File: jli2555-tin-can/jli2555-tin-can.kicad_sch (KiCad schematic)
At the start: 20 parts, among them J2 AudioJack3, U1 OPA134, U2 TL072

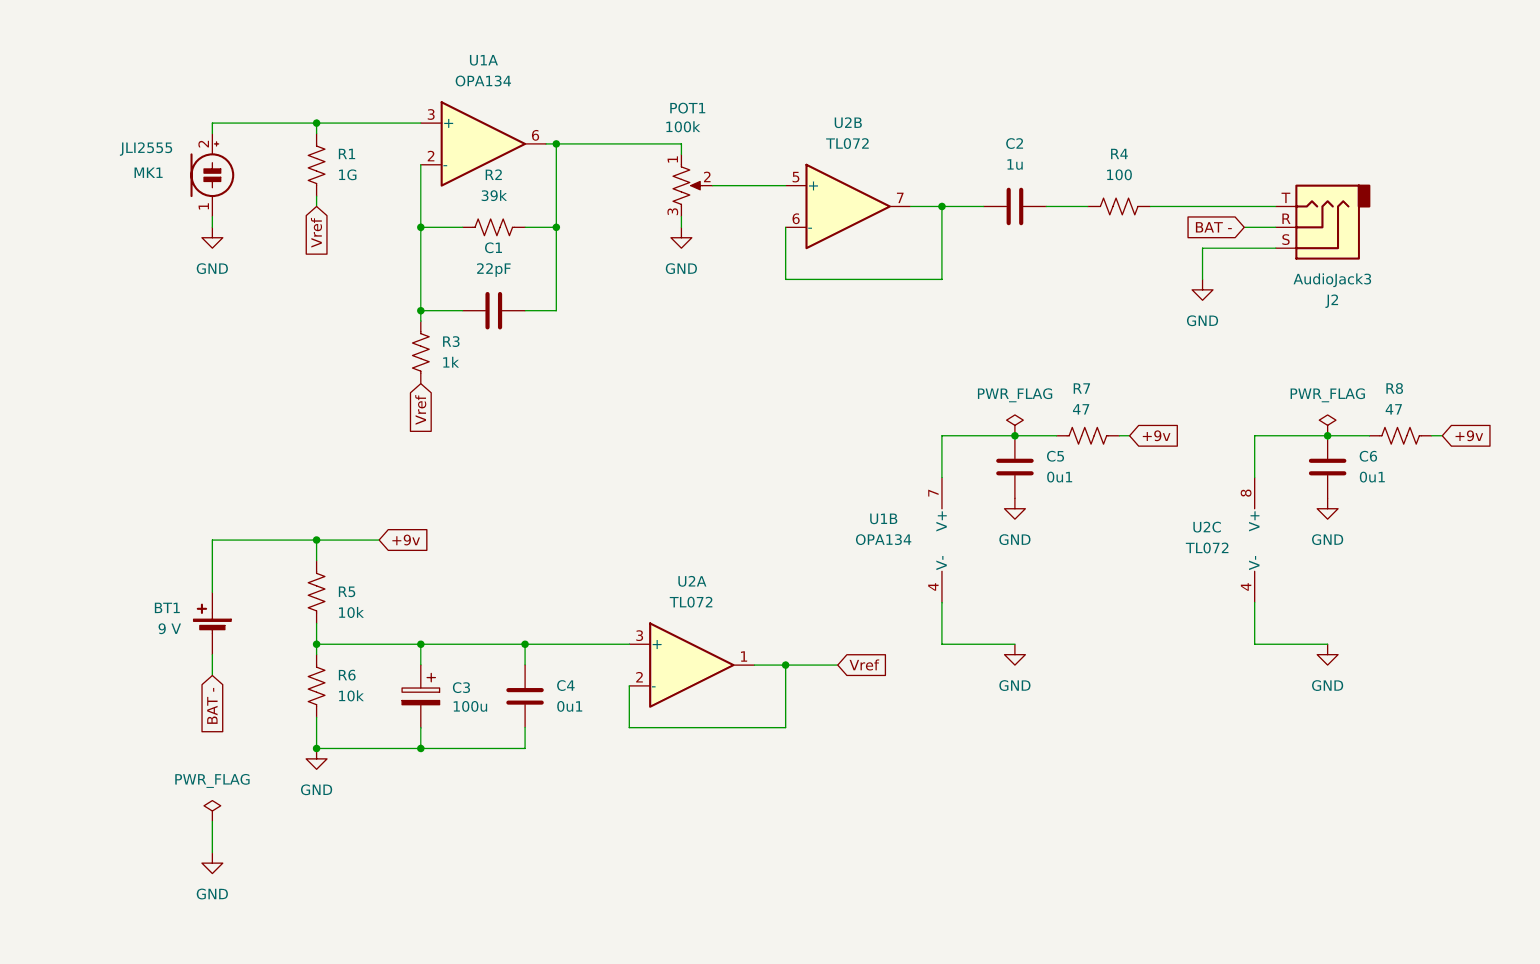
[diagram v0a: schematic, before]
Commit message: finalize the -9v powered circuit design. Renamed entire project
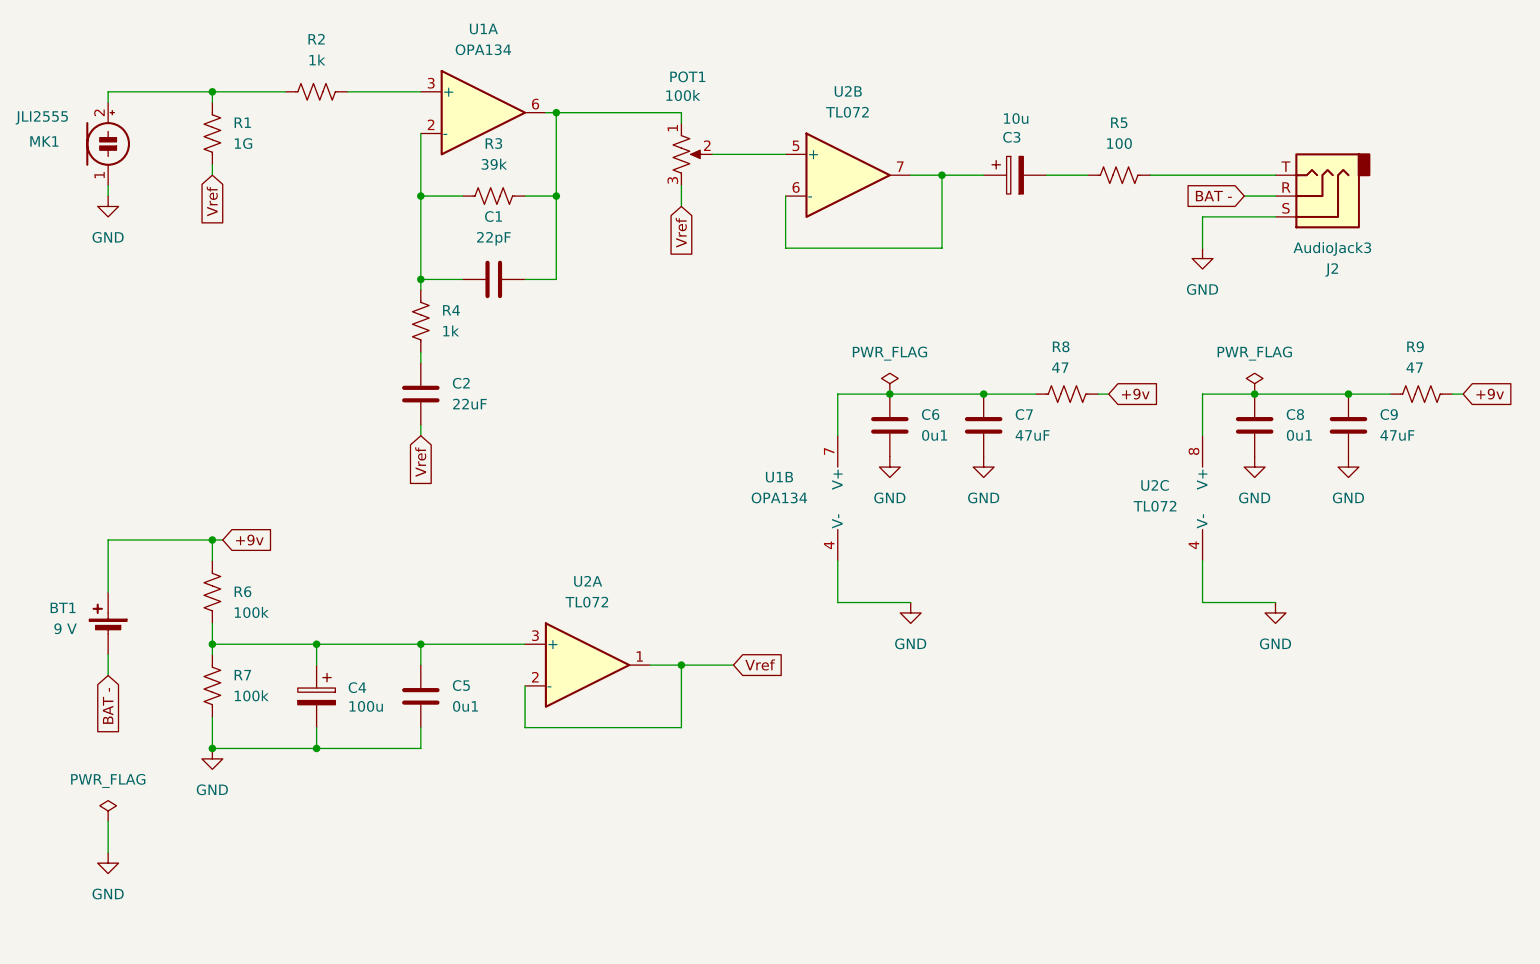
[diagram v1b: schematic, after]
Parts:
- added C3: 10u, Capacitor_THT:CP_Radial_D5.0mm_P2.50mm, symbol Device:C_Polarized
- added C7, C9: 47uF, Capacitor_THT:C_Disc_D5.0mm_W2.5mm_P2.50mm, symbol Device:C
- added R2: 1k, Resistor_THT:R_Axial_DIN0207_L6.3mm_D2.5mm_P10.16mm_Horizontal, symbol Device:R_US
- C2: value 1u -> 22uF; footprint Capacitor_THT:C_Rect_L7.2mm_W4.5mm_P5.00mm_FKS2_FKP2_MKS2_MKP2 -> Capacitor_THT:C_Disc_D5.0mm_W2.5mm_P2.50mm
- R6: renamed from R5; value 10k -> 100k
- R7: renamed from R6; value 10k -> 100k
- renumbered C3 to C4, C4 to C5, C5 to C6, C6 to C8, R2 to R3, R3 to R4, R4 to R5, R7 to R8, R8 to R9
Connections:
- net GND: now also C7.1, C9.1; no longer POT1.3
- net Vref: now also C2.1, POT1.3; no longer R4.2
- net at C8.2, R9.1, U2.8 (V+): now also C9.2
- net at MK1.2 (+), R1.1: now also R2.1; no longer U1.3 (+)
- net at C2.2: now also R4.2; no longer R5.1
- net at U2.6 (-), U2.7: now also C3.1; no longer C2.1
- net at C6.2, R8.1, U1.7 (V+): now also C7.2
- new net: C3.2, R5.1
- new net: R2.2, U1.3 (+)
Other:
- title: JLI 2555 tin can mic  -> JLI 2555 tin can microphone
- moved on the sheet: BT1, C1, C4, C5, C6, C8, J2, MK1, POT1, R1, R3, R4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

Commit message: Finalization of the first printed prototype, revision 1
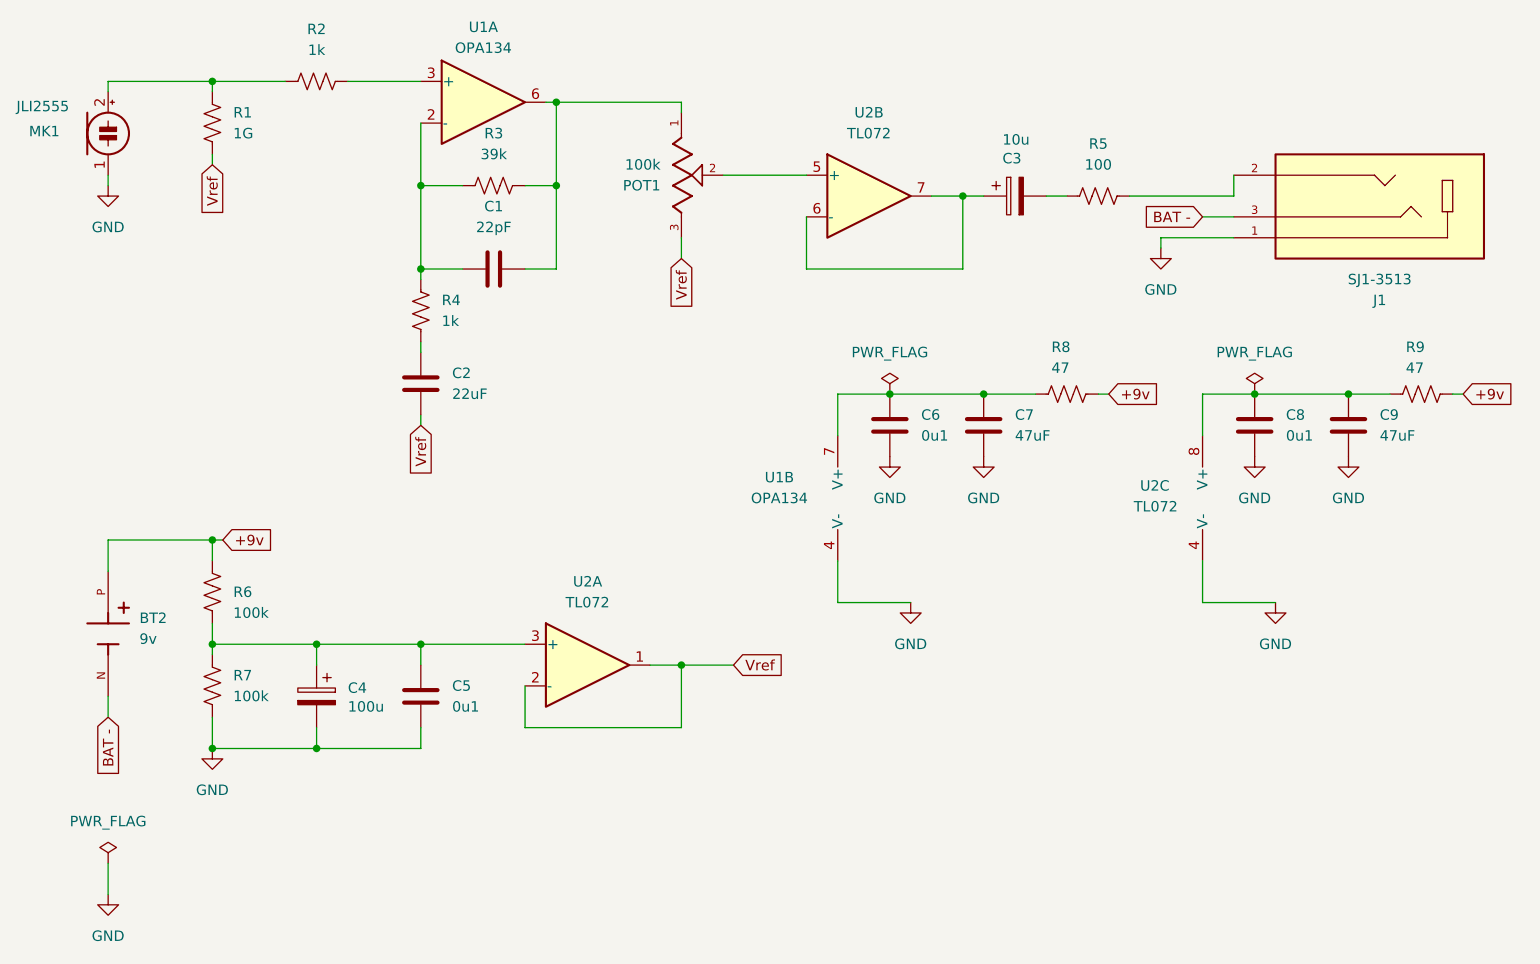
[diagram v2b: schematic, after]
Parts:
- removed BT1: 9 V, Battery:BatteryHolder_MPD_BA9VPC_1xPP3, symbol Device:Battery_Cell
- removed J2: AudioJack3, Connector_Audio:Jack_3.5mm_CUI_SJ1-3513N_Horizontal, symbol Connector_Audio:AudioJack3
- removed POT1: 100k, Potentiometer_THT:Potentiometer_Alps_RK09Y11_Single_Horizontal, symbol Device:R_Potentiometer_US
- added BT2: 9v, 1294:BAT_1294, symbol 1294:1294
- added J1: SJ1-3513, SJ1-3513:CUI_SJ1-3513, symbol SJ1-3513:SJ1-3513
- added POT1: 100k, PTN16_A100120K1A1:POT_PTN16-A100120K1A1, symbol PTN16-A100120K1A1:PTN16-A100120K1A1
- C5: footprint Capacitor_THT:C_Disc_D5.0mm_W2.5mm_P5.00mm -> Capacitor_THT:C_Disc_D5.0mm_W2.5mm_P2.50mm
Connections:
- net +9v: now also BT2.P
- net BAT -: now also BT2.N, J1.3
- net GND: now also J1.1
- net Vref: now also POT1.3
- net at R5.2: now also J1.2
- net at C1.2, R3.2, U1.6: now also POT1.1
- net at U2.5 (+): now also POT1.2
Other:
- moved on the sheet: C1, C2, C3, MK1, R1, R2, R3, R4, R5, U1A, U2B
